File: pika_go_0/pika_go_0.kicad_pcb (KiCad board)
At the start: 4 copper layers, 50 x 110 mm, 110 parts, among them J1 BAT, J2 MCU_DEBUG, J3 Micro_SD_Card_Det1, J4 Conn_01x02, J5 LCD, J6 USB_C_Receptacle_USB2.0_16P, J7 MIC, J8 SPK, Q1 BSS138, SW1 PWR, SW2 LSN, SW3 PTT, SW4 UP, SW5 DOWN, SW6 LEFT, SW7 RIGHT, U1 TPS610333DRLR, U10 MAX4467EKA_T, U2 BQ25895RTW, U3 MCP1703Ax-330xxMB, U4 STM32H733VGTx, U5 USB3300-EZK, U6 MCP1703Ax-500xxTT, U7 E22-900M30S, U8 CAM-M8Q-0, U9 SSM2305RMZ-REEL7, Y1 SG-210STF 24.0000ML0

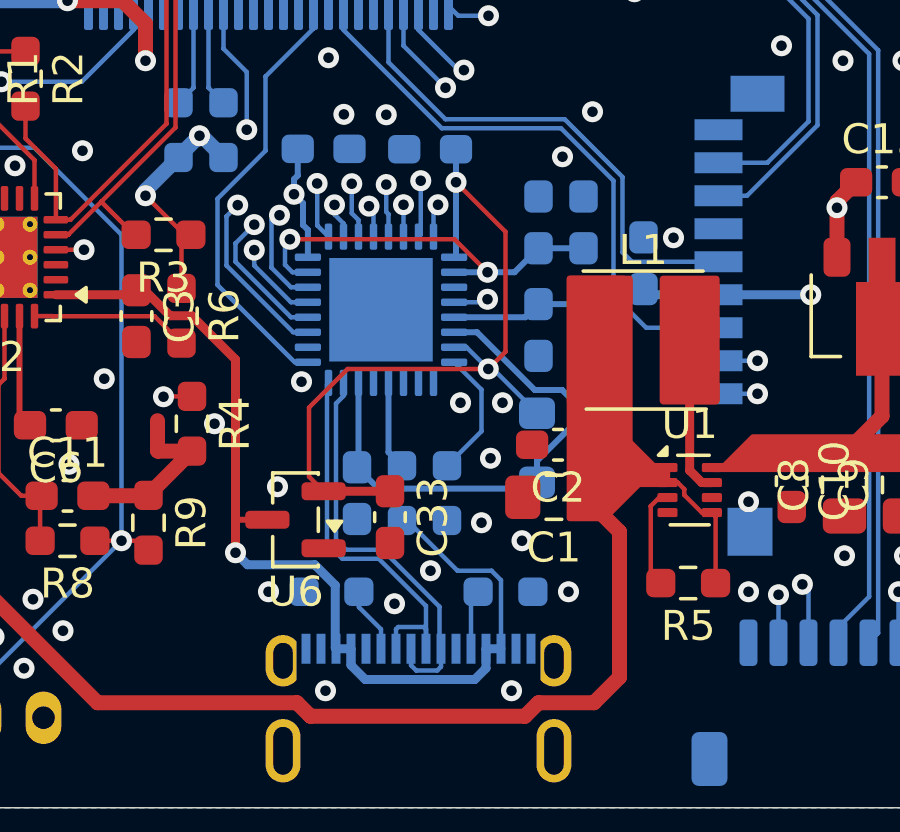
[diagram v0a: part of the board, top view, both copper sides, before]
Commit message: USB PHY routing fix
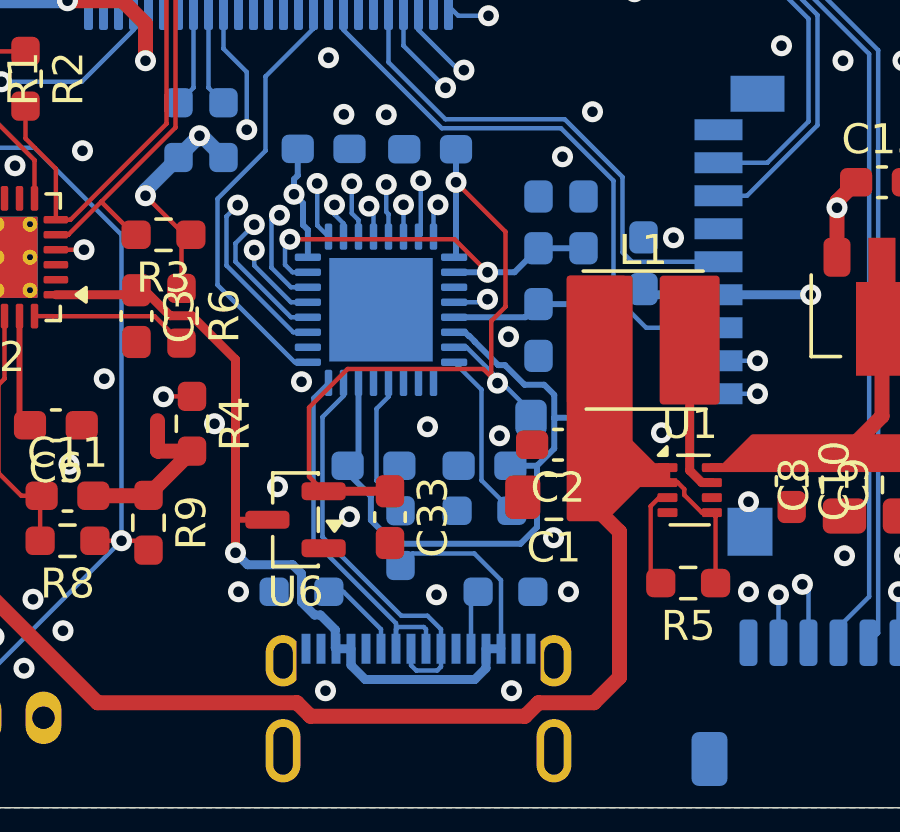
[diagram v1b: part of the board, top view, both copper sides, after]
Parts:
- moved C29 3.47 mm to (57.2, 131.6), turned to 180 degrees
- moved R17 1.50 mm to (54.4, 134.0)
- moved R18 1.38 mm to (57.2, 133.1), turned to 180 degrees
- moved FB2 1.38 mm to (59.9, 130.0), turned to 0 degrees
- moved C30 1.07 mm to (53.5, 131.6), turned to 0 degrees
- moved R20 1.00 mm to (51.1, 135.8)
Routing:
- net /USB/USB_VDDA3.3: track 17.6 -> 22.4 mm
- net Net-(U5-VBUS): track 2.95 -> 4.76 mm
- net Net-(U5-RBIAS): track 4.30 -> 5.75 mm
- net /USB/USB_VDD3.3: track 37.0 -> 38.3 mm
- net /USB/USB_DM: track 13.3 -> 12.6 mm
- net USB_VBUS: track 33.9 -> 33.3 mm

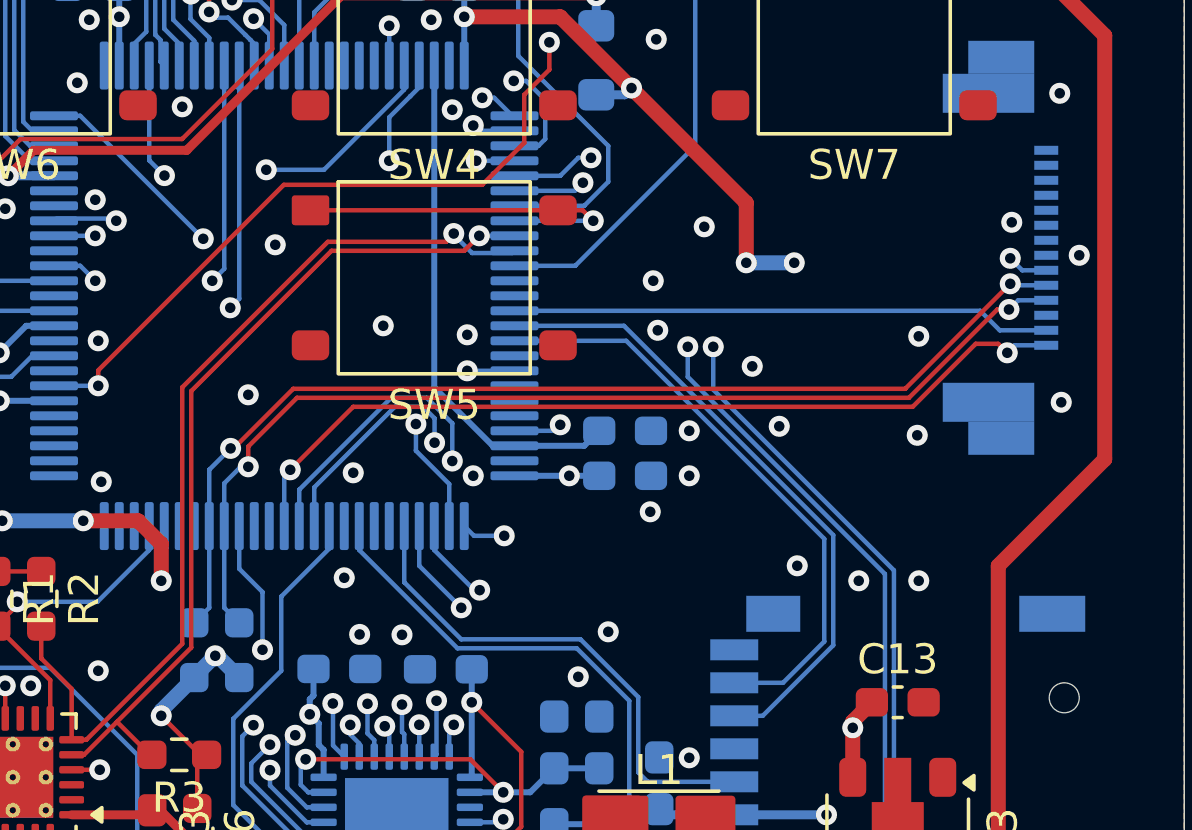
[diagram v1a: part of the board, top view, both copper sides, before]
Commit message: Button DN moved
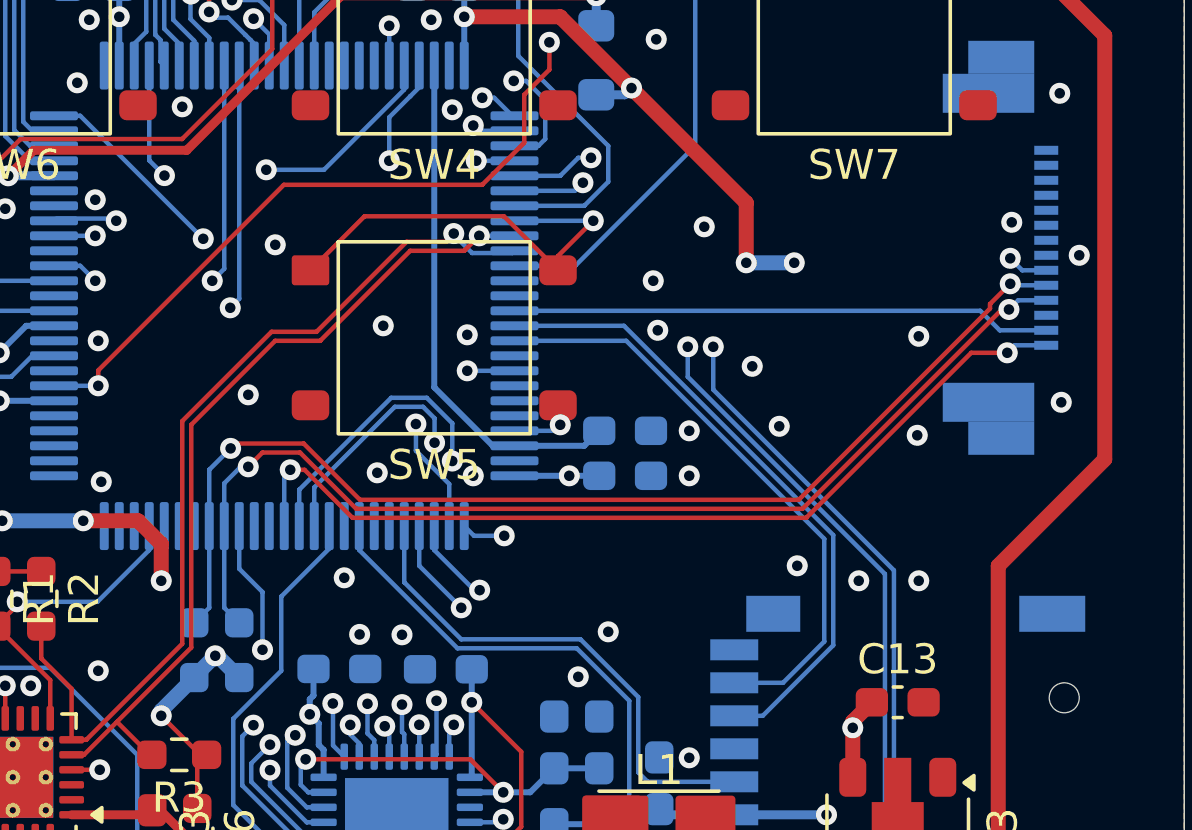
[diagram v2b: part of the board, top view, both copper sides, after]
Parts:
- moved SW5 2.00 mm to (55.0, 110.0)
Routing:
- net /MCU/BTN_DOWN: track 12.2 -> 14.5 mm
- net /MCU/LCD_I2C_SDA: track 35.8 -> 37.5 mm
- net /MCU/LCD_I2C_SCL: track 35.2 -> 36.3 mm
- net /MCU/LCD_COMSCN: track 29.1 -> 30.2 mm
- net CHG_I2C_SCL: track 28.6 -> 27.9 mm
- net CHG_I2C_SDA: track 31.3 -> 30.6 mm
- net GND: vias 161 -> 160
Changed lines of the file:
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@@
 	(footprint "Pika:TE_STSA"
 		(layer "F.Cu")
-		(at 55 108)
+		(at 55 110)
 		(descr "Tactile switch, 6.2x6.2mm, gullwing leads, https://www.te.com/commerce/DocumentDelivery/DDEController?Action=srchrtrv&DocNm=ALCOSWITCH_Sealed_Tactile_Switches&DocType=Data%20Sheet&DocLang=English&DocFormat=pdf&PartCntxt=2506469-3")
 		(tags "TE STSA")
@@
 	)
 	(via
-		(at 62.2 115.8)
-		(size 0.7)
-		(drill 0.35)
-		(layers "F.Cu" "B.Cu")
-		(free yes)
-		(net "GND")
-	)
-	(via
 		(at 64 72.2)
 		(size 0.7)
@@
 	)
 	(via
-		(at 52.3 114.5)
+		(at 53.1 114.5)
 		(size 0.7)
 		(drill 0.35)
@@
 	)
 	(segment
-		(start 59.95 105.75)
-		(end 59.125 105.75)
+		(start 57.325 105.95)
+		(end 59.125 107.75)
 		(width 0.15)
 		(layer "F.Cu")
@@
 	)
 	(segment
-		(start 50.875 105.75)
-		(end 59.125 105.75)
+		(start 52.675 105.95)
+		(end 57.325 105.95)
+		(width 0.15)
+		(layer "F.Cu")
+		(net "/MCU/BTN_DOWN")
+	)
+	(segment
+		(start 59.125 107.275)
+		(end 59.125 107.75)
+		(width 0.15)
+		(layer "F.Cu")
+		(net "/MCU/BTN_DOWN")
+	)
+	(segment
+		(start 50.875 107.75)
+		(end 52.675 105.95)
 		(width 0.15)
 		(layer "F.Cu")
@@
 	(segment
 		(start 60.3 106.1)
-		(end 59.95 105.75)
+		(end 59.125 107.275)
 		(width 0.15)
 		(layer "F.Cu")
@@
 	)
 	(segment
-		(start 51.575736 107.1)
-		(end 56 107.1)
+		(start 56 107.1)
+		(end 56.5 106.6)
 		(width 0.15)
 		(layer "F.Cu")
@@
 	)
 	(segment
-		(start 44.424632 122.800367)
-		(end 43.324999 123.9)
+		(start 54.2 107.1)
+		(end 56 107.1)
 		(width 0.15)
 		(layer "F.Cu")
@@
 	)
 	(segment
-		(start 45.5875 123.9)
-		(end 45.524265 123.9)
+		(start 49.7 110.1)
+		(end 51.2 110.1)
 		(width 0.15)
 		(layer "F.Cu")
@@
 	)
 	(segment
-		(start 46.9 120.324999)
-		(end 46.9 111.775736)
+		(start 51.2 110.1)
+		(end 54.2 107.1)
 		(width 0.15)
 		(layer "F.Cu")
@@
 	)
 	(segment
-		(start 45.524265 123.9)
-		(end 44.424632 122.800367)
+		(start 44.424632 122.800367)
+		(end 43.324999 123.9)
 		(width 0.15)
 		(layer "F.Cu")
@@
 	)
 	(segment
-		(start 43.324999 123.9)
-		(end 42.9125 123.9)
+		(start 45.5875 123.9)
+		(end 45.524265 123.9)
 		(width 0.15)
 		(layer "F.Cu")
@@
 	)
 	(segment
-		(start 56 107.1)
-		(end 56.5 106.6)
+		(start 46.9 120.324999)
+		(end 46.9 112.9)
 		(width 0.15)
 		(layer "F.Cu")
@@
 	)
 	(segment
-		(start 46.9 111.775736)
-		(end 51.575736 107.1)
+		(start 46.9 112.9)
+		(end 49.7 110.1)
+		(width 0.15)
+		(layer "F.Cu")
+		(net "CHG_I2C_SCL")
+	)
+	(segment
+		(start 45.524265 123.9)
+		(end 44.424632 122.800367)
+		(width 0.15)
+		(layer "F.Cu")
+		(net "CHG_I2C_SCL")
+	)
+	(segment
+		(start 43.324999 123.9)
+		(end 42.9125 123.9)
 		(width 0.15)
 		(layer "F.Cu")
@@
 	)
 	(segment
-		(start 55.4 106.8)
-		(end 51.451472 106.8)
+		(start 41.9 119.6125)
+		(end 41.9 120.688236)
 		(width 0.15)
 		(layer "F.Cu")
@@
 	)
 	(segment
-		(start 41.9 119.6125)
-		(end 41.9 120.688236)
+		(start 46.6 120.200735)
+		(end 43.400735 123.4)
+		(width 0.15)
+		(layer "F.Cu")
+		(net "CHG_I2C_SDA")
+	)
+	(segment
+		(start 51.075736 109.8)
+		(end 49.575736 109.8)
 		(width 0.15)
 		(layer "F.Cu")
@@
 	)
 	(segment
-		(start 51.451472 106.8)
-		(end 46.6 111.651472)
+		(start 55.4 106.8)
+		(end 54.075736 106.8)
 		(width 0.15)
 		(layer "F.Cu")
@@
 	)
 	(segment
-		(start 46.6 111.651472)
-		(end 46.6 120.200735)
+		(start 43.400735 123.4)
+		(end 42.9125 123.4)
 		(width 0.15)
 		(layer "F.Cu")
@@
 	)
 	(segment
-		(start 55.649997 106.550003)
-		(end 55.4 106.8)
+		(start 54.075736 106.8)
+		(end 51.075736 109.8)
 		(width 0.15)
 		(layer "F.Cu")
@@
 	)
 	(segment
-		(start 42.9125 121.700736)
-		(end 42.9125 123.4)
+		(start 49.575736 109.8)
+		(end 46.6 112.775736)
 		(width 0.15)
 		(layer "F.Cu")
@@
 	)
 	(segment
-		(start 41.9 120.688236)
-		(end 42.9125 121.700736)
+		(start 55.649997 106.550003)
+		(end 55.4 106.8)
 		(width 0.15)
 		(layer "F.Cu")
@@
 	)
 	(segment
-		(start 43.400735 123.4)
+		(start 46.6 112.775736)
+		(end 46.6 120.200735)
+		(width 0.15)
+		(layer "F.Cu")
+		(net "CHG_I2C_SDA")
+	)
+	(segment
+		(start 42.9125 121.700736)
 		(end 42.9125 123.4)
 		(width 0.15)
@@
 	)
 	(segment
-		(start 46.6 120.200735)
-		(end 43.400735 123.4)
+		(start 41.9 120.688236)
+		(end 42.9125 121.700736)
 		(width 0.15)
 		(layer "F.Cu")
@@
 	)
 	(segment
-		(start 74.1 110.5)
-		(end 73.8 110.2)
+		(start 52.275736 116)
+		(end 50.675736 114.4)
 		(width 0.15)
 		(layer "F.Cu")
@@
 	)
 	(segment
-		(start 70.948528 112.3)
-		(end 52.3 112.3)
+		(start 67.4 116)
+		(end 52.275736 116)
 		(width 0.15)
 		(layer "F.Cu")
@@
 	)
 	(segment
-		(start 73.8 110.2)
-		(end 73.048528 110.2)
+		(start 72.9 110.5)
+		(end 67.4 116)
 		(width 0.15)
 		(layer "F.Cu")
@@
 	)
 	(segment
-		(start 52.3 112.3)
+		(start 50.675736 114.4)
 		(end 50.2 114.4)
 		(width 0.15)
@@
 	)
 	(segment
-		(start 73.048528 110.2)
-		(end 70.948528 112.3)
+		(start 74.1 110.5)
+		(end 72.9 110.5)
 		(width 0.15)
 		(layer "F.Cu")
@@
 	)
 	(segment
-		(start 73.767677 109.056587)
-		(end 74.156587 109.056587)
+		(start 74.156587 109.056587)
+		(end 73.919149 109.056587)
 		(width 0.15)
 		(layer "F.Cu")
@@
 	)
 	(segment
-		(start 48.8 113.624264)
-		(end 50.424264 112)
+		(start 52.4 115.7)
+		(end 50.525 113.825)
 		(width 0.15)
 		(layer "F.Cu")
@@
 	)
 	(segment
-		(start 50.424264 112)
-		(end 70.824264 112)
+		(start 73.919149 109.056587)
+		(end 67.275736 115.7)
 		(width 0.15)
 		(layer "F.Cu")
@@
 	)
 	(segment
-		(start 70.824264 112)
-		(end 73.767677 109.056587)
+		(start 49.275 113.825)
+		(end 48.8 114.3)
 		(width 0.15)
 		(layer "F.Cu")
@@
 	)
 	(segment
-		(start 48.8 114.3)
-		(end 48.8 113.624264)
+		(start 67.275736 115.7)
+		(end 52.4 115.7)
+		(width 0.15)
+		(layer "F.Cu")
+		(net "/MCU/LCD_I2C_SCL")
+	)
+	(segment
+		(start 50.525 113.825)
+		(end 49.275 113.825)
 		(width 0.15)
 		(layer "F.Cu")
@@
 	)
 	(segment
-		(start 70.7 111.7)
-		(end 74.2 108.2)
+		(start 74.2 108.2)
+		(end 73.525736 108.874264)
+		(width 0.15)
+		(layer "F.Cu")
+		(net "/MCU/LCD_I2C_SDA")
+	)
+	(segment
+		(start 48.373187 113.525)
+		(end 48.211879 113.686308)
+		(width 0.15)
+		(layer "F.Cu")
+		(net "/MCU/LCD_I2C_SDA")
+	)
+	(segment
+		(start 67.151472 115.4)
+		(end 52.524264 115.4)
 		(width 0.15)
 		(layer "F.Cu")
@@
 	)
 	(segment
-		(start 48.313692 113.686308)
-		(end 50.3 111.7)
+		(start 52.524264 115.4)
+		(end 50.649264 113.525)
+		(width 0.15)
+		(layer "F.Cu")
+		(net "/MCU/LCD_I2C_SDA")
+	)
+	(segment
+		(start 73.525736 109.025736)
+		(end 67.151472 115.4)
+		(width 0.15)
+		(layer "F.Cu")
+		(net "/MCU/LCD_I2C_SDA")
+	)
+	(segment
+		(start 50.649264 113.525)
+		(end 48.373187 113.525)
 		(width 0.15)
 		(layer "F.Cu")
@@
 	)
 	(segment
-		(start 50.3 111.7)
-		(end 70.7 111.7)
+		(start 73.525736 108.874264)
+		(end 73.525736 109.025736)
 		(width 0.15)
 		(layer "F.Cu")

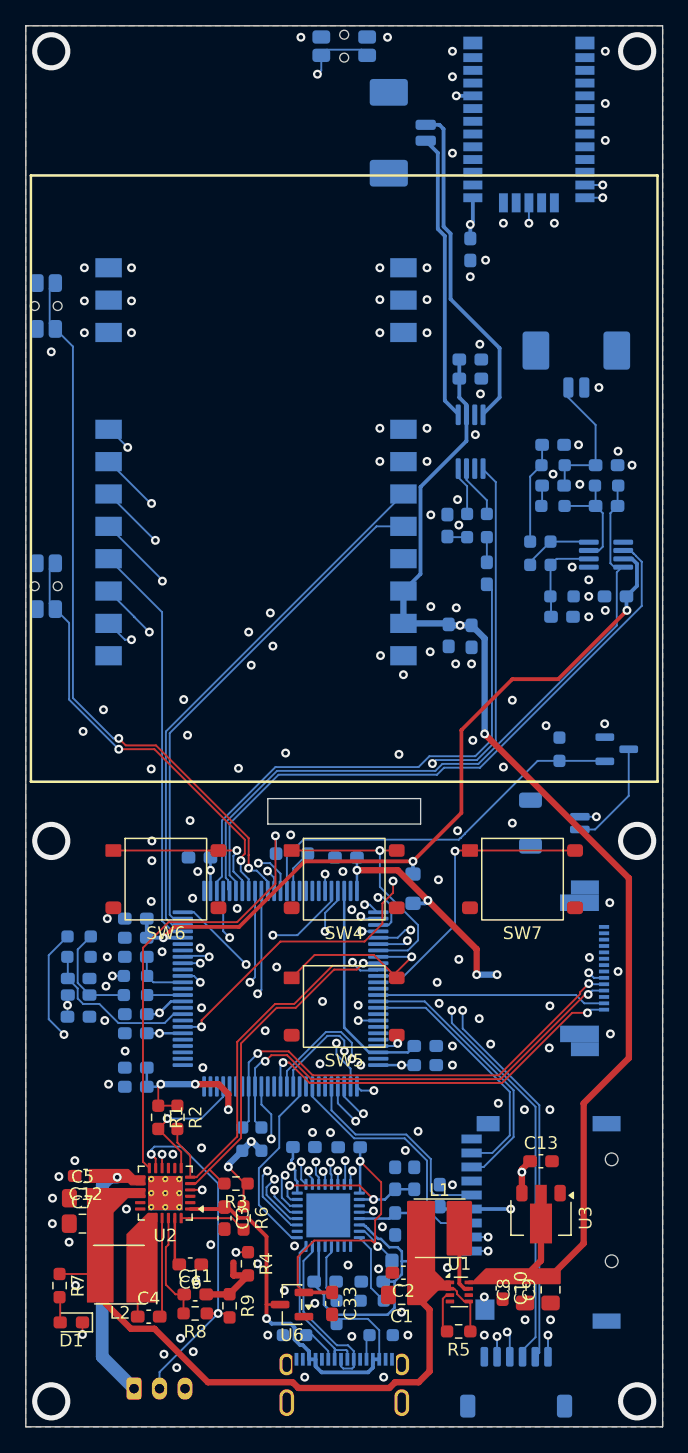
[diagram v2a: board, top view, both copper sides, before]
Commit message: LCD connectors moved, traces cleanup
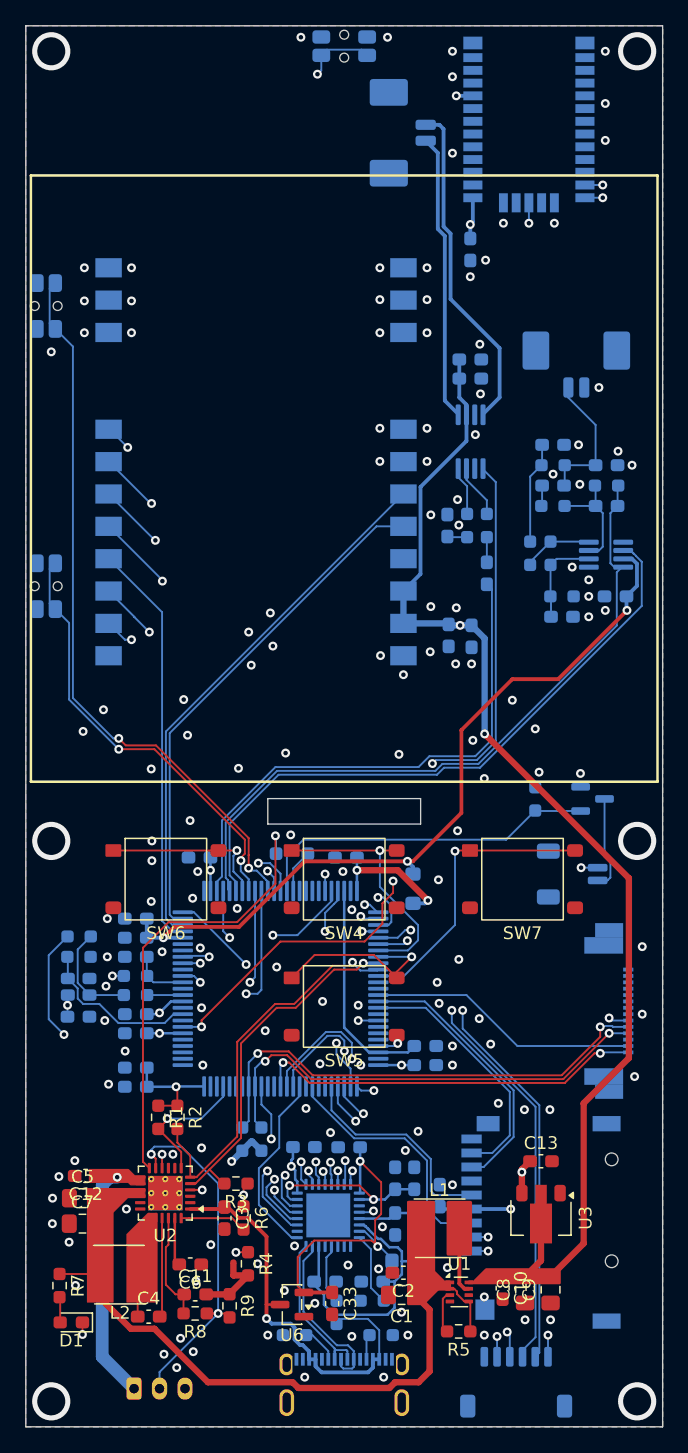
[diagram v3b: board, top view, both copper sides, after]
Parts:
- moved Q1 4.34 mm to (74.5, 93.7)
- moved R14 4.34 mm to (70.0, 93.7)
- moved J4 4.24 mm to (72.9, 99.6)
- moved J5 3.85 mm to (74.9, 110.3)
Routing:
- net +3.3V: track 72.4 -> 56.5 mm, vias 22 -> 18
- net /MCU/LCD_BKLT: track 30.8 -> 27.3 mm
- net /MCU/LCD_RST: track 18.0 -> 21.3 mm
- net USB_PHY_CLK: track 40.9 -> 42.4 mm
- net USB_ULPI_D2: track 26.2 -> 27.4 mm
- net Net-(J4-Pin_1): track 8.59 -> 7.46 mm
- net USB_ULPI_D0: track 27.5 -> 28.4 mm
- net /MCU/LCD_I2C_SDA: track 37.5 -> 38.4 mm
- net SPK_EN: track 45.8 -> 45.1 mm
- net /MCU/LCD_I2C_SCL: track 36.3 -> 36.8 mm
- net /MCU/LCD_COMSCN: track 30.2 -> 30.7 mm
- net GND: vias 160 -> 156

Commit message: Silk screen cleanup, various fixes after DRC
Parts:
- J4: value Conn_01x02 -> BKLT
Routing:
- net /MCU/SWDIO: track 30.1 -> 31.9 mm
- net GND: vias 156 -> 158
- net +5V: vias 2 -> 1
